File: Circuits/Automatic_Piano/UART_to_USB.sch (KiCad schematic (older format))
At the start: 10 parts

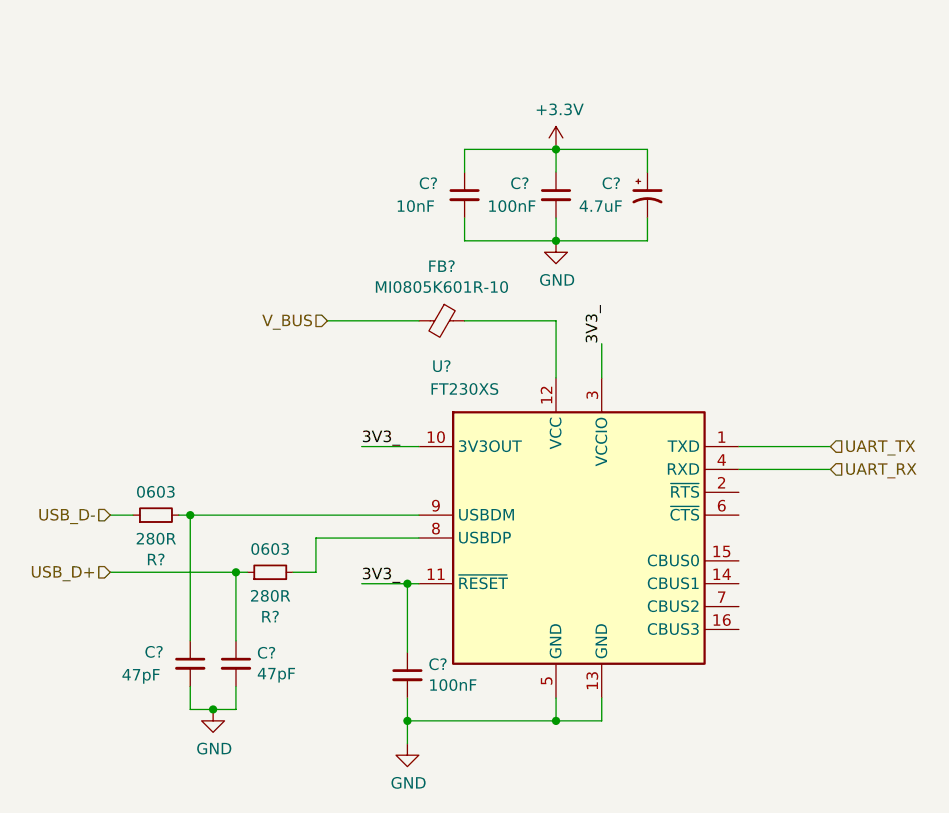
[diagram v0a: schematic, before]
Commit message: Main Piano MIDI receiver completed. Might want indicator LEDS and more peripherals.
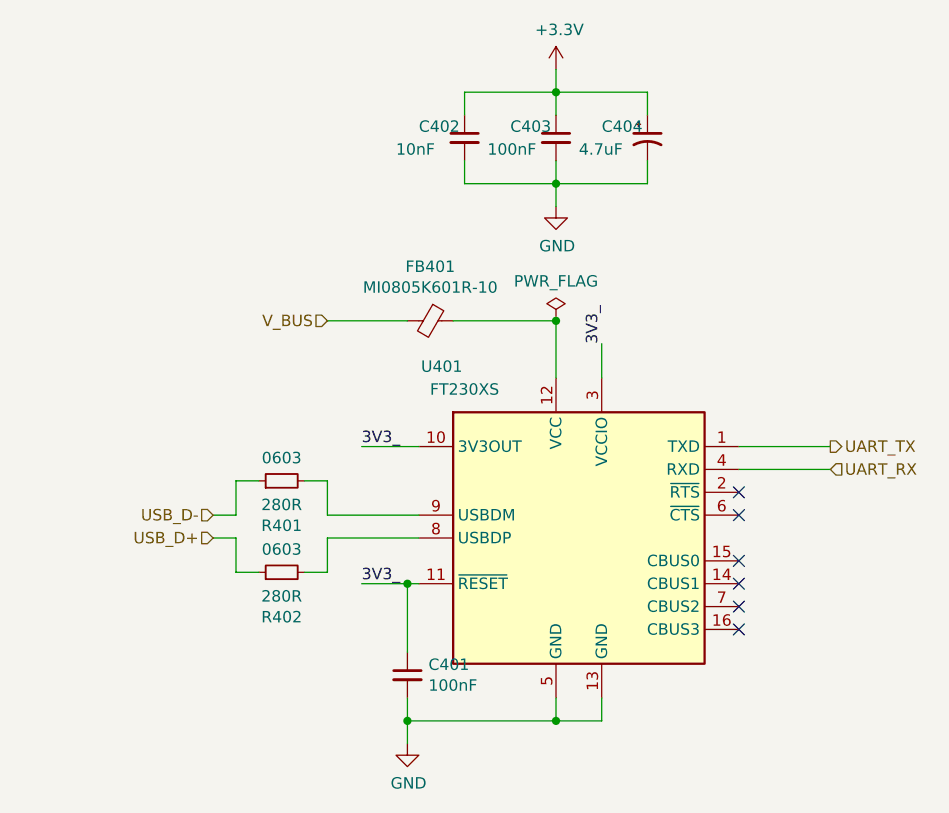
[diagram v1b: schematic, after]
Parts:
- removed C? (x2): 47pF, symbol Device:C_Small
- gave numbers to parts that had none: 8
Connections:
- no-connect marks 0 -> 6
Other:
- moved on the sheet: C402, C403, C404, FB401, R401, R402
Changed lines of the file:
@@
 $EndDescr
 $Comp
-L Interface_USB:FT230XS U?
+L Interface_USB:FT230XS U401
 U 1 1 5E1F9DE9
 P 5900 3150
-F 0 "U?" H 5300 3900 50  0000 C CNN
+F 0 "U401" H 5300 3900 50  0000 C CNN
 F 1 "FT230XS" H 5400 3800 50  0000 C CNN
 F 2 "Package_SO:SSOP-16_3.9x4.9mm_P0.635mm" H 6900 2550 50  0001 C CNN
@@
 Text HLabel 4800 2200 0    50   Input ~ 0
 V_BUS
-Text HLabel 3850 3050 0    50   Input ~ 0
+Text HLabel 4300 3050 0    50   Input ~ 0
 USB_D-
-Text HLabel 3850 3300 0    50   Input ~ 0
+Text HLabel 4300 3150 0    50   Input ~ 0
 USB_D+
-Text HLabel 7000 2750 2    50   Input ~ 0
+Text HLabel 7000 2750 2    50   Output ~ 0
 UART_TX
 Text HLabel 7000 2850 2    50   Input ~ 0
@@
 L Device:R_Small R?
 U 1 1 5E231173
-P 4050 3050
+P 4600 2900
 AR Path="/5E18C714/5E231173" Ref="R?"  Part="1"
-AR Path="/5E18D7E6/5E231173" Ref="R?"  Part="1"
-F 0 "R?" V 3854 3050 50  0000 C CNN
-F 1 "280R" V 3945 3050 50  0000 C CNN
-F 2 "Resistor_SMD:R_0603_1608Metric" H 4050 3050 50  0001 C CNN
-F 3 "~" H 4050 3050 50  0001 C CNN
-F 4 "0603" V 4150 3050 50  0000 C CNN "FootprintField"
-	1    4050 3050
+AR Path="/5E18D7E6/5E231173" Ref="R401"  Part="1"
+F 0 "R401" V 4404 2900 50  0000 C CNN
+F 1 "280R" V 4495 2900 50  0000 C CNN
+F 2 "Resistor_SMD:R_0603_1608Metric" H 4600 2900 50  0001 C CNN
+F 3 "~" H 4600 2900 50  0001 C CNN
+F 4 "0603" V 4700 2900 50  0000 C CNN "FootprintField"
+	1    4600 2900
 	0    -1   -1   0
 $EndComp
@@
 L Device:R_Small R?
 U 1 1 5E231233
-P 4550 3300
+P 4600 3300
 AR Path="/5E18C714/5E231233" Ref="R?"  Part="1"
-AR Path="/5E18D7E6/5E231233" Ref="R?"  Part="1"
-F 0 "R?" V 4354 3300 50  0000 C CNN
-F 1 "280R" V 4445 3300 50  0000 C CNN
-F 2 "Resistor_SMD:R_0603_1608Metric" H 4550 3300 50  0001 C CNN
-F 3 "~" H 4550 3300 50  0001 C CNN
-F 4 "0603" V 4650 3300 50  0000 C CNN "FootprintField"
-	1    4550 3300
+AR Path="/5E18D7E6/5E231233" Ref="R402"  Part="1"
+F 0 "R402" V 4404 3300 50  0000 C CNN
+F 1 "280R" V 4495 3300 50  0000 C CNN
+F 2 "Resistor_SMD:R_0603_1608Metric" H 4600 3300 50  0001 C CNN
+F 3 "~" H 4600 3300 50  0001 C CNN
+F 4 "0603" V 4700 3300 50  0000 C CNN "FootprintField"
+	1    4600 3300
 	0    -1   -1   0
 $EndComp
 $Comp
-L Device:C_Small C?
-U 1 1 5E234381
-P 4400 3700
-F 0 "C?" H 4492 3746 50  0000 L CNN
-F 1 "47pF" H 4492 3655 50  0000 L CNN
-F 2 "" H 4400 3700 50  0001 C CNN
-F 3 "~" H 4400 3700 50  0001 C CNN
-	1    4400 3700
-	1    0    0    -1
-$EndComp
-$Comp
-L Device:Ferrite_Bead_Small FB?
+L Device:Ferrite_Bead_Small FB401
 U 1 1 5E235485
-P 5300 2200
-F 0 "FB?" V 5063 2200 50  0000 C CNN
-F 1 "MI0805K601R-10" V 5154 2200 50  0000 C CNN
-F 2 "Resistor_SMD:R_0805_2012Metric" V 5230 2200 50  0001 C CNN
-F 3 "~" H 5300 2200 50  0001 C CNN
-	1    5300 2200
+P 5250 2200
+F 0 "FB401" V 5013 2200 50  0000 C CNN
+F 1 "MI0805K601R-10" V 5104 2200 50  0000 C CNN
+F 2 "Resistor_SMD:R_0805_2012Metric" V 5180 2200 50  0001 C CNN
+F 3 "~" H 5250 2200 50  0001 C CNN
+	1    5250 2200
 	0    1    1    0
 $EndComp
-$Comp
-L Device:C_Small C?
-U 1 1 5E23B800
-P 4200 3700
-F 0 "C?" H 4000 3750 50  0000 L CNN
-F 1 "47pF" H 3900 3650 50  0000 L CNN
-F 2 "" H 4200 3700 50  0001 C CNN
-F 3 "~" H 4200 3700 50  0001 C CNN
-	1    4200 3700
-	1    0    0    -1
-$EndComp
-Wire Wire Line
-	4150 3050 4200 3050
-Wire Wire Line
-	3950 3050 3850 3050
-Wire Wire Line
-	4450 3300 4400 3300
-Wire Wire Line
-	4650 3300 4750 3300
-Wire Wire Line
-	4750 3300 4750 3150
-Wire Wire Line
-	4750 3150 5200 3150
-Wire Wire Line
-	4200 3600 4200 3050
-Connection ~ 4200 3050
-Wire Wire Line
-	4200 3050 5200 3050
-Wire Wire Line
-	4400 3600 4400 3300
-Connection ~ 4400 3300
-Wire Wire Line
-	4400 3300 3850 3300
-Wire Wire Line
-	4200 3800 4200 3900
-Wire Wire Line
-	4200 3900 4300 3900
-Wire Wire Line
-	4400 3900 4400 3800
-$Comp
-L power:GND #PWR?
-U 1 1 5E23DA0A
-P 4300 3900
-AR Path="/5E18C714/5E23DA0A" Ref="#PWR?"  Part="1"
-AR Path="/5E18D7E6/5E23DA0A" Ref="#PWR?"  Part="1"
-F 0 "#PWR?" H 4300 3650 50  0001 C CNN
-F 1 "GND" H 4305 3727 50  0000 C CNN
-F 2 "" H 4300 3900 50  0001 C CNN
-F 3 "" H 4300 3900 50  0001 C CNN
-	1    4300 3900
-	1    0    0    -1
-$EndComp
-Wire Wire Line
-	4800 2200 5200 2200
-Wire Wire Line
-	5400 2200 5800 2200
-$Comp
-L power:+3.3V #PWR?
-U 1 1 5E23F4D2
-P 5800 1450
-AR Path="/5E18C714/5E23F4D2" Ref="#PWR?"  Part="1"
-AR Path="/5E23F4D2" Ref="#PWR?"  Part="1"
-AR Path="/5E18D7E6/5E23F4D2" Ref="#PWR?"  Part="1"
-F 0 "#PWR?" H 5800 1300 50  0001 C CNN
-F 1 "+3.3V" H 5815 1623 50  0000 C CNN
-F 2 "" H 5800 1450 50  0001 C CNN
-F 3 "" H 5800 1450 50  0001 C CNN
-	1    5800 1450
-	1    0    0    -1
-$EndComp
+Wire Wire Line
+	4700 3300 4800 3300
+Wire Wire Line
+	4800 3300 4800 3150
+Wire Wire Line
+	4800 3150 5200 3150
+Wire Wire Line
+	4800 2200 5150 2200
+Wire Wire Line
+	5350 2200 5800 2200
 $Comp
 L power:GND #PWR?
 U 1 1 5E241DFA
-P 5800 1850
+P 5800 1700
 AR Path="/5E18C714/5E241DFA" Ref="#PWR?"  Part="1"
-AR Path="/5E18D7E6/5E241DFA" Ref="#PWR?"  Part="1"
-F 0 "#PWR?" H 5800 1600 50  0001 C CNN
-F 1 "GND" H 5805 1677 50  0000 C CNN
-F 2 "" H 5800 1850 50  0001 C CNN
-F 3 "" H 5800 1850 50  0001 C CNN
-	1    5800 1850
-	1    0    0    -1
-$EndComp
-$Comp
-L Device:C_Small C?
+AR Path="/5E18D7E6/5E241DFA" Ref="#PWR0403"  Part="1"
+F 0 "#PWR0403" H 5800 1450 50  0001 C CNN
+F 1 "GND" H 5805 1527 50  0000 C CNN
+F 2 "" H 5800 1700 50  0001 C CNN
+F 3 "" H 5800 1700 50  0001 C CNN
+	1    5800 1700
+	1    0    0    -1
+$EndComp
+$Comp
+L Device:C_Small C402
 U 1 1 5E242457
-P 5400 1650
-F 0 "C?" H 5200 1700 50  0000 L CNN
-F 1 "10nF" H 5100 1600 50  0000 L CNN
-F 2 "" H 5400 1650 50  0001 C CNN
-F 3 "~" H 5400 1650 50  0001 C CNN
-	1    5400 1650
-	1    0    0    -1
-$EndComp
-$Comp
-L Device:C_Small C?
+P 5400 1400
+F 0 "C402" H 5200 1450 50  0000 L CNN
+F 1 "10nF" H 5100 1350 50  0000 L CNN
+F 2 "" H 5400 1400 50  0001 C CNN
+F 3 "~" H 5400 1400 50  0001 C CNN
+	1    5400 1400
+	1    0    0    -1
+$EndComp
+$Comp
+L Device:C_Small C403
 U 1 1 5E243DDA
-P 5800 1650
-F 0 "C?" H 5600 1700 50  0000 L CNN
-F 1 "100nF" H 5500 1600 50  0000 L CNN
-F 2 "" H 5800 1650 50  0001 C CNN
-F 3 "~" H 5800 1650 50  0001 C CNN
-	1    5800 1650
-	1    0    0    -1
-$EndComp
-Wire Wire Line
-	5400 1750 5400 1850
-Wire Wire Line
-	5800 1750 5800 1850
-Wire Wire Line
-	6200 1850 6200 1750
-Connection ~ 5800 1850
-Wire Wire Line
-	5800 1850 6200 1850
-Wire Wire Line
-	5400 1850 5800 1850
-Wire Wire Line
-	5400 1550 5400 1450
-Wire Wire Line
-	5400 1450 5800 1450
-Wire Wire Line
-	5800 1450 6200 1450
-Wire Wire Line
-	6200 1450 6200 1550
-Connection ~ 5800 1450
-Wire Wire Line
-	5800 1550 5800 1450
+P 5800 1400
+F 0 "C403" H 5600 1450 50  0000 L CNN
+F 1 "100nF" H 5500 1350 50  0000 L CNN
+F 2 "" H 5800 1400 50  0001 C CNN
+F 3 "~" H 5800 1400 50  0001 C CNN
+	1    5800 1400
+	1    0    0    -1
+$EndComp
+Wire Wire Line
+	5400 1500 5400 1600
+Wire Wire Line
+	5800 1500 5800 1600
+Wire Wire Line
+	6200 1600 6200 1500
+Connection ~ 5800 1600
+Wire Wire Line
+	5800 1600 6200 1600
+Wire Wire Line
+	5400 1600 5800 1600
+Wire Wire Line
+	5400 1300 5400 1200
+Wire Wire Line
+	6200 1200 6200 1300
 Wire Wire Line
 	5800 2200 5800 2450
-Connection ~ 4300 3900
-Wire Wire Line
-	4300 3900 4400 3900
 Wire Wire Line
 	6000 2450 6000 2300
@@
 3V3_
 $Comp
-L Device:C_Small C?
+L Device:C_Small C401
 U 1 1 5E27C7CF
 P 5150 3750
-F 0 "C?" H 5242 3796 50  0000 L CNN
+F 0 "C401" H 5242 3796 50  0000 L CNN
 F 1 "100nF" H 5242 3705 50  0000 L CNN
 F 2 "" H 5150 3750 50  0001 C CNN
@@
 	5150 3350 4950 3350
 $Comp
-L Device:CP1_Small C?
+L Device:CP1_Small C404
 U 1 1 5E27DED4
-P 6200 1650
-F 0 "C?" H 6000 1700 50  0000 L CNN
-F 1 "4.7uF" H 5900 1600 50  0000 L CNN
-F 2 "" H 6200 1650 50  0001 C CNN
-F 3 "~" H 6200 1650 50  0001 C CNN
-	1    6200 1650
+P 6200 1400
+F 0 "C404" H 6000 1450 50  0000 L CNN
+F 1 "4.7uF" H 5900 1350 50  0000 L CNN
+F 2 "" H 6200 1400 50  0001 C CNN
+F 3 "~" H 6200 1400 50  0001 C CNN
+	1    6200 1400
 	1    0    0    -1
 $EndComp
@@
 P 5150 4050
 AR Path="/5E18C714/5E280E4D" Ref="#PWR?"  Part="1"
-AR Path="/5E18D7E6/5E280E4D" Ref="#PWR?"  Part="1"
-F 0 "#PWR?" H 5150 3800 50  0001 C CNN
+AR Path="/5E18D7E6/5E280E4D" Ref="#PWR0401"  Part="1"
+F 0 "#PWR0401" H 5150 3800 50  0001 C CNN
 F 1 "GND" H 5155 3877 50  0000 C CNN
 F 2 "" H 5150 4050 50  0001 C CNN
@@
 Wire Wire Line
 	6600 2850 7000 2850
+NoConn ~ 6600 2950
+NoConn ~ 6600 3050
+NoConn ~ 6600 3250
+NoConn ~ 6600 3350
+NoConn ~ 6600 3450
+NoConn ~ 6600 3550
+Wire Wire Line
+	4300 3150 4400 3150
+Wire Wire Line
+	4400 3150 4400 3300
+Wire Wire Line
+	4400 3300 4500 3300
+Wire Wire Line
+	4300 3050 4400 3050
+Wire Wire Line
+	4400 3050 4400 2900
+Wire Wire Line
+	4400 2900 4500 2900
+Wire Wire Line
+	4700 2900 4800 2900
+Wire Wire Line
+	4800 2900 4800 3050
+Wire Wire Line
+	4800 3050 5200 3050
+Wire Wire Line
+	5800 1300 5800 1200
+Connection ~ 5800 1200
+Wire Wire Line
+	5800 1200 6200 1200
+Wire Wire Line
+	5400 1200 5800 1200
+$Comp
+L power:+3.3V #PWR?
+U 1 1 5E23F4D2
+P 5800 1100
+AR Path="/5E18C714/5E23F4D2" Ref="#PWR?"  Part="1"
+AR Path="/5E23F4D2" Ref="#PWR?"  Part="1"
+AR Path="/5E18D7E6/5E23F4D2" Ref="#PWR0402"  Part="1"
+F 0 "#PWR0402" H 5800 950 50  0001 C CNN
+F 1 "+3.3V" H 5815 1273 50  0000 C CNN
+F 2 "" H 5800 1100 50  0001 C CNN
+F 3 "" H 5800 1100 50  0001 C CNN
+	1    5800 1100
+	1    0    0    -1
+$EndComp
+Wire Wire Line
+	5800 1100 5800 1200
+Wire Wire Line
+	5800 1600 5800 1700
+$Comp
+L power:PWR_FLAG #FLG0401
+U 1 1 5E254F65
+P 5800 2200
+F 0 "#FLG0401" H 5800 2275 50  0001 C CNN
+F 1 "PWR_FLAG" H 5800 2373 50  0000 C CNN
+F 2 "" H 5800 2200 50  0001 C CNN
+F 3 "~" H 5800 2200 50  0001 C CNN
+	1    5800 2200
+	1    0    0    -1
+$EndComp
+Connection ~ 5800 2200
 $EndSCHEMATC
